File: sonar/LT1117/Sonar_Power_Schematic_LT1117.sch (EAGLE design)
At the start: 30 parts, among them U1 LT3471', U2 LT1962-5, U4 LT1175

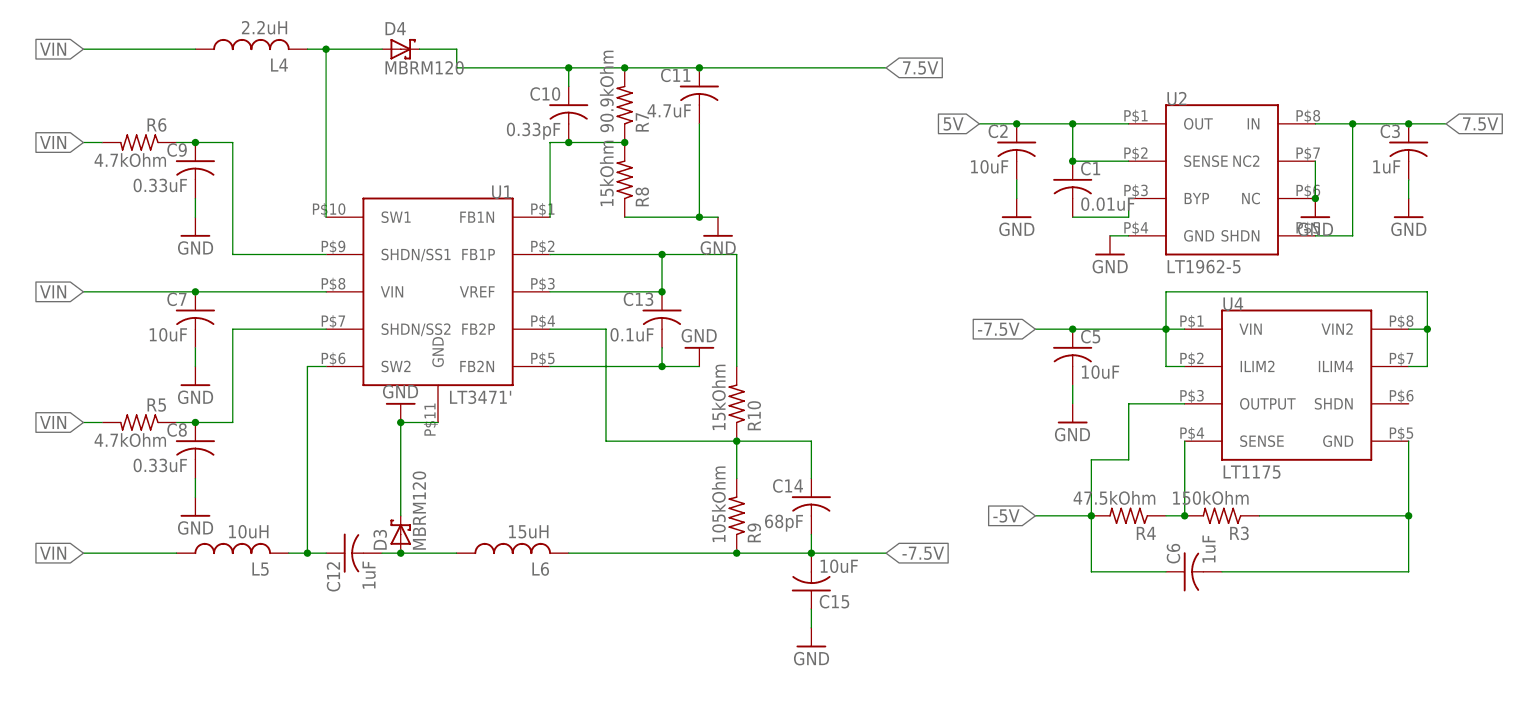
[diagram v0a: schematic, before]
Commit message: LT1117 and LT1962 schematics, PCBs, and design blocks
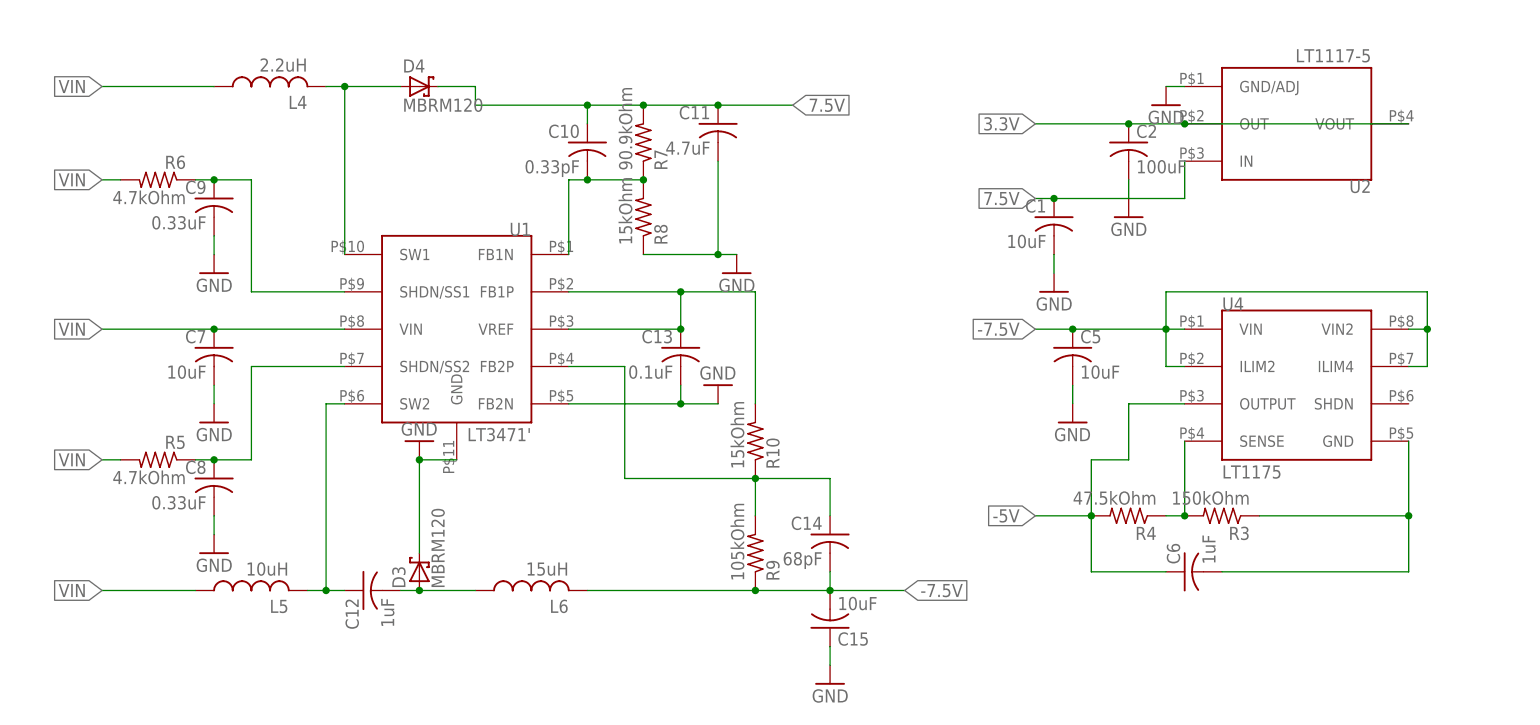
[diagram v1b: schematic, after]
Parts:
- removed C3: 1uF, adafruit:C-USC0603
- C1: value 0.01uF -> 10uF
- C2: value 10uF -> 100uF; device adafruit:C-USC0603 -> adafruit:C-USC1210
- U2: value LT1962-5 -> LT1117-5; device Moira:LT1962-5 -> Moira:LT1117-5
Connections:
- removed net 5V: C1.1, C2.1, U2.OUT, U2.SENSE
- removed net N$4: C1.2, U2.BYP
- new net 3.3V: C2.1, U2.OUT, U2.VOUT
- net 7.5V: now also C1.1; no longer C3.1, U2.SHDN
- net GND: now also C1.2, U2.GND/ADJ; no longer C3.2, U2.GND, U2.NC, U2.NC2
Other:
- moved on the sheet: C1, C10, C11, C12, C13, C14, C15, C2, C7, C8, C9, D3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

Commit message: GND fixed
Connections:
- removed net N$10: C6.2, R3.1, U4.GND
- net GND: now also C6.2, R3.1, U4.GND
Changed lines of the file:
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@@
 <part name="C2" library="adafruit" library_urn="urn:adsk.eagle:library:420" deviceset="C-US" device="C1210" value="100uF"/>
 <part name="GND3" library="supply1" library_urn="urn:adsk.eagle:library:371" deviceset="GND" device=""/>
+<part name="GND4" library="supply1" library_urn="urn:adsk.eagle:library:371" deviceset="GND" device=""/>
 </parts>
 <sheets>
@@
 <instance part="C2" gate="G$1" x="48.26" y="27.94"/>
 <instance part="GND3" gate="1" x="48.26" y="17.78" rot="MR0"/>
+<instance part="GND4" gate="1" x="86.36" y="-33.02" rot="MR0"/>
 </instances>
 <busses>
@@
 <wire x1="48.26" y1="22.86" x2="48.26" y2="20.32" width="0.1524" layer="91"/>
 </segment>
+<segment>
+<pinref part="R3" gate="G$1" pin="1"/>
+<wire x1="66.04" y1="-22.86" x2="86.36" y2="-22.86" width="0.1524" layer="91"/>
+<pinref part="U4" gate="G$1" pin="GND"/>
+<wire x1="86.36" y1="-22.86" x2="86.36" y2="-12.7" width="0.1524" layer="91"/>
+<pinref part="C6" gate="G$1" pin="2"/>
+<wire x1="60.96" y1="-30.48" x2="86.36" y2="-30.48" width="0.1524" layer="91"/>
+<wire x1="86.36" y1="-30.48" x2="86.36" y2="-22.86" width="0.1524" layer="91"/>
+<junction x="86.36" y="-22.86"/>
+<pinref part="GND4" gate="1" pin="GND"/>
+<junction x="86.36" y="-30.48"/>
+</segment>
 </net>
 <net name="-5V" class="0">
@@
 </segment>
 </net>
-<net name="N$10" class="0">
-<segment>
-<pinref part="R3" gate="G$1" pin="1"/>
-<wire x1="66.04" y1="-22.86" x2="86.36" y2="-22.86" width="0.1524" layer="91"/>
-<pinref part="U4" gate="G$1" pin="GND"/>
-<wire x1="86.36" y1="-22.86" x2="86.36" y2="-12.7" width="0.1524" layer="91"/>
-<pinref part="C6" gate="G$1" pin="2"/>
-<wire x1="60.96" y1="-30.48" x2="86.36" y2="-30.48" width="0.1524" layer="91"/>
-<wire x1="86.36" y1="-30.48" x2="86.36" y2="-22.86" width="0.1524" layer="91"/>
-<junction x="86.36" y="-22.86"/>
-</segment>
-</net>
